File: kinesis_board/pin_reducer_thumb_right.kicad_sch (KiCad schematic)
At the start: 2 parts

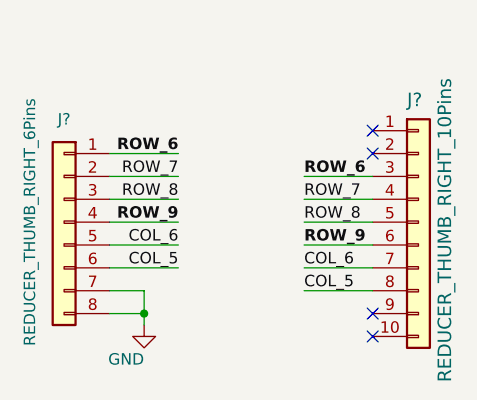
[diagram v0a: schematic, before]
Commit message: removed properties in schematics and updated kicad project version
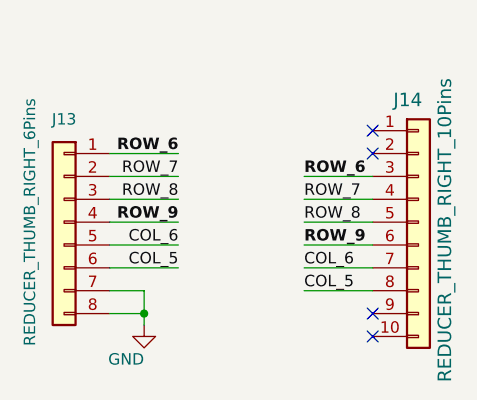
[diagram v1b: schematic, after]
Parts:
- gave numbers to parts that had none: 2
